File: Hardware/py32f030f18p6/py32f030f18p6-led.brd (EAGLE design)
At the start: 81.3 x 81.3 mm, 132 parts, among them IC2 AP2114HA-3.3TRG1, J10 455-1750-1-ND, J11 455-1750-1-ND, J12 455-1750-1-ND, J14 USB_MINI-B_SMT, J15 455-1750-1-ND, J16 455-1750-1-ND, J9 455-1750-1-ND, Q1 MMBT3904LT3G, Q10 MMBT3904LT3G, Q11 MMBT3904LT3G, Q12 MMBT3904LT3G, Q13 MMBT3904LT3G, Q14 MMBT3904LT3G, Q15 MMBT3904LT3G, Q16 MMBT3904LT3G, Q17 MMBT3904LT3G, Q18 MMBT3904LT3G, Q19 MMBT3904LT3G, Q2 MMBT3904LT3G, Q20 MMBT3904LT3G, Q21 MMBT3904LT3G, Q22 MMBT3904LT3G, Q23 MMBT3904LT3G, Q24 MMBT3904LT3G, Q25 MMBT3904LT3G, Q26 MMBT3904LT3G, Q27 MMBT3904LT3G, Q28 MMBT3904LT3G, Q29 MMBT3904LT3G, Q3 MMBT3904LT3G, Q30 MMBT3904LT3G, Q31 MMBT3904LT3G, Q32 MMBT3904LT3G, Q4 MMBT3904LT3G, Q5 MMBT3904LT3G, Q6 MMBT3904LT3G, Q7 MMBT3904LT3G, Q8 MMBT3904LT3G, Q9 MMBT3904LT3G, U1 TC74HC595AF(EL,F), U2 TC74HC595AF(EL,F), U3 TC74HC595AF(EL,F), U4 TC74HC595AF(EL,F), U5 TC74HC595AF(EL,F), U6 TC74HC595AF(EL,F), U7 TC74HC595AF(EL,F), U8 TC74HC595AF(EL,F)

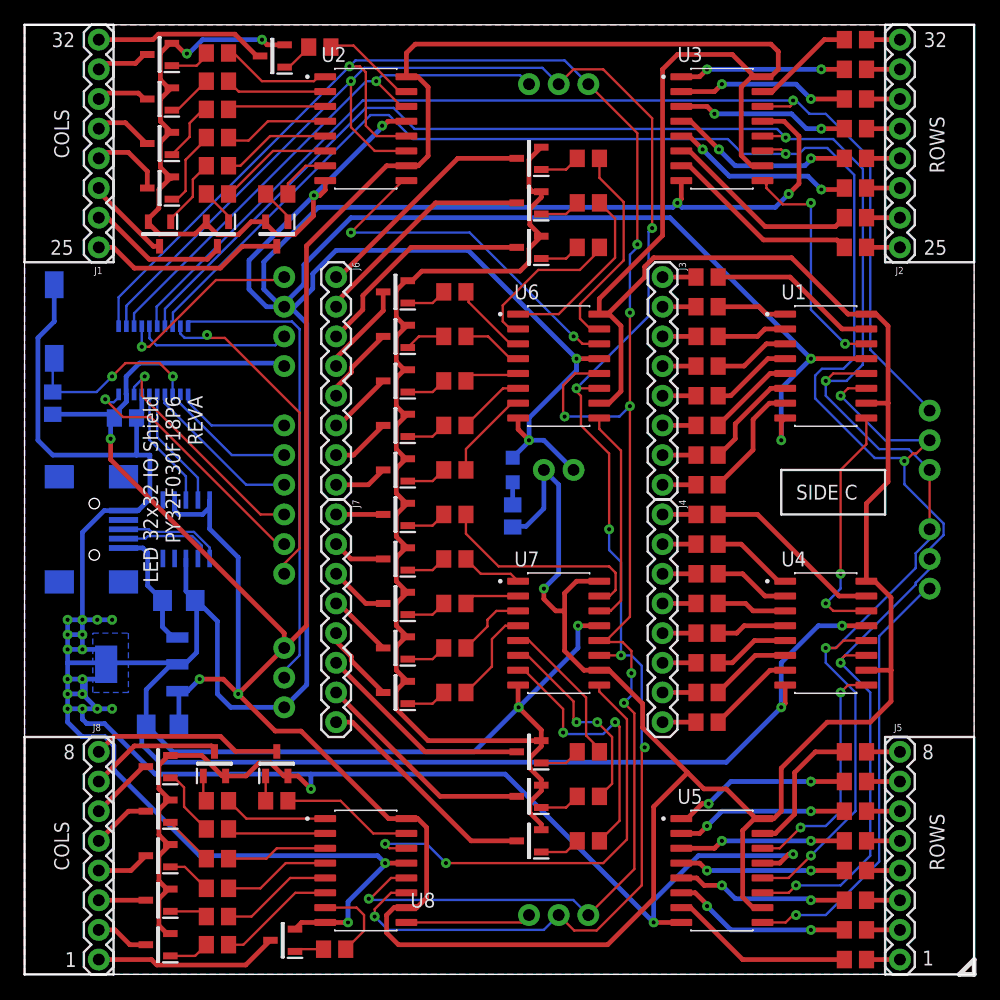
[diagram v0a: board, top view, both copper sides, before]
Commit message: Got row/col reversed
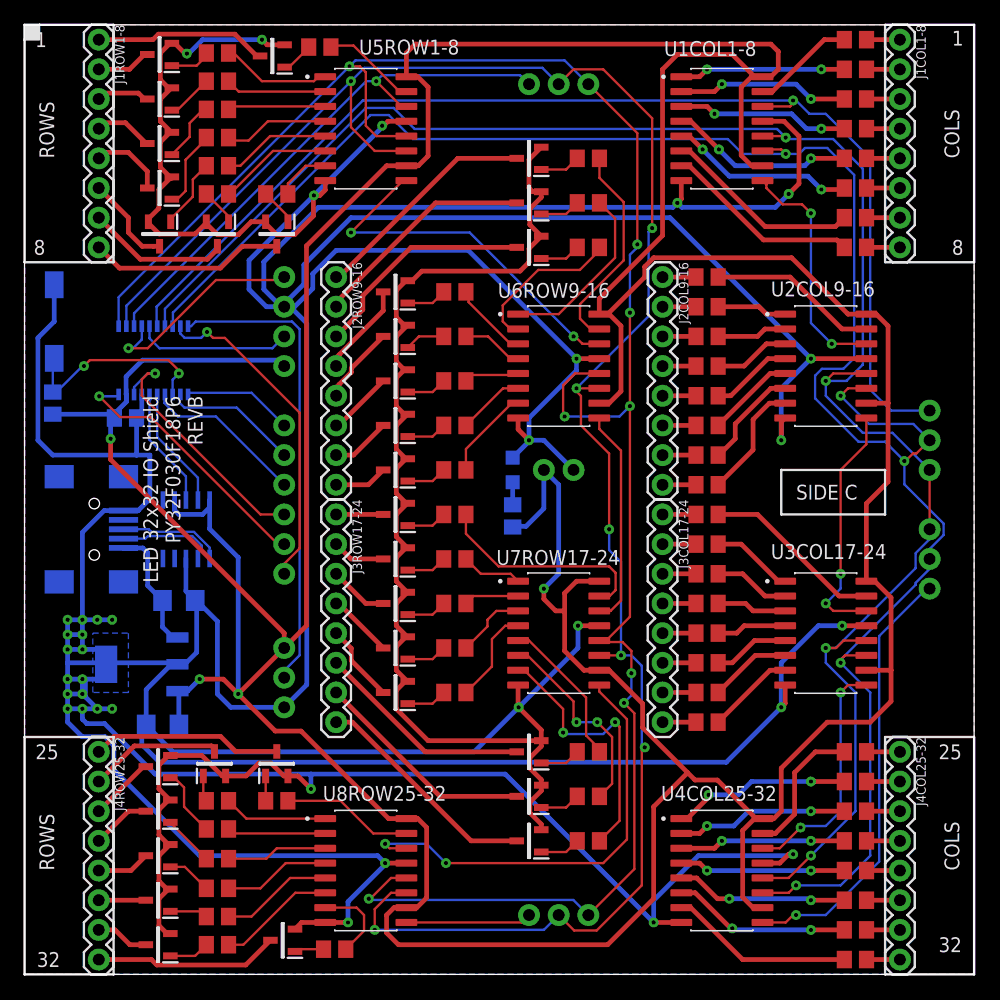
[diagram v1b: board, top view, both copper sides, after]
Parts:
- renumbered J1 to J1ROW1-8, J2 to J1COL1-8, J3 to J2COL9-16, J4 to J3COL17-24, J5 to J4COL25-32, J6 to J2ROW9-16, J7 to J3ROW17-24, J8 to J4ROW25-32, U1 to U2COL9-16, U2 to U5ROW1-8, U3 to U1COL1-8, U4 to U3COL17-24, U5 to U4COL25-32, U6 to U6ROW9-16, U7 to U7ROW17-24, U8 to U8ROW25-32
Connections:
- net COL_SCLK_IN renamed ROW_SCLK_IN
- net ROW_SLCK_IN renamed COL_SLCK_IN
- net COL_DATA_IN: now also J9.1, U$2.16, U1COL1-8.14; no longer J11.1, U$2.13, U5ROW1-8.14
- net COL_RCLK_IN: now also J10.3, J9.3, U$2.17, U1COL1-8.12, U2COL9-16.12, U3COL17-24.12, U4COL25-32.12; no longer J11.3, J12.3, U$2.11, U5ROW1-8.12, U6ROW9-16.12, U7ROW17-24.12, U8ROW25-32.12
- net ROW_DATA_IN: now also J11.1, U$2.13, U5ROW1-8.14; no longer J9.1, U$2.16, U1COL1-8.14
- net ROW_RCLK_IN: now also J11.3, J12.3, U$2.11, U5ROW1-8.12, U6ROW9-16.12, U7ROW17-24.12, U8ROW25-32.12; no longer J10.3, J9.3, U$2.17, U1COL1-8.12, U2COL9-16.12, U3COL17-24.12, U4COL25-32.12
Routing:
- net COL_DATA_IN: track 47.1 -> 100.7 mm
- net ROW_DATA_IN: track 98.8 -> 47.1 mm
- net ROW_RCLK_IN: track 158.1 -> 176.5 mm, vias 4 -> 8
- net COL_RCLK_IN: track 176.5 -> 158.1 mm, vias 8 -> 4
- net PA13-SWDIO: track 16.4 -> 18.5 mm
- net GPIO4: track 20.1 -> 22.1 mm
- net PF2-NRST: track 16.3 -> 17.5 mm
- net GPIO5: track 22.1 -> 22.9 mm
- net ROW_SCLK_IN: track 172.7 -> 173.4 mm
- net N$6: track 7.46 -> 8.02 mm
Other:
- board text added: "LED 32x32 IO Shield PY32F030F18P6 REVB"
- board text removed: "LED 32x32 IO Shield PY32F030F18P6 REVA"

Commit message: Added rx/tx breakout
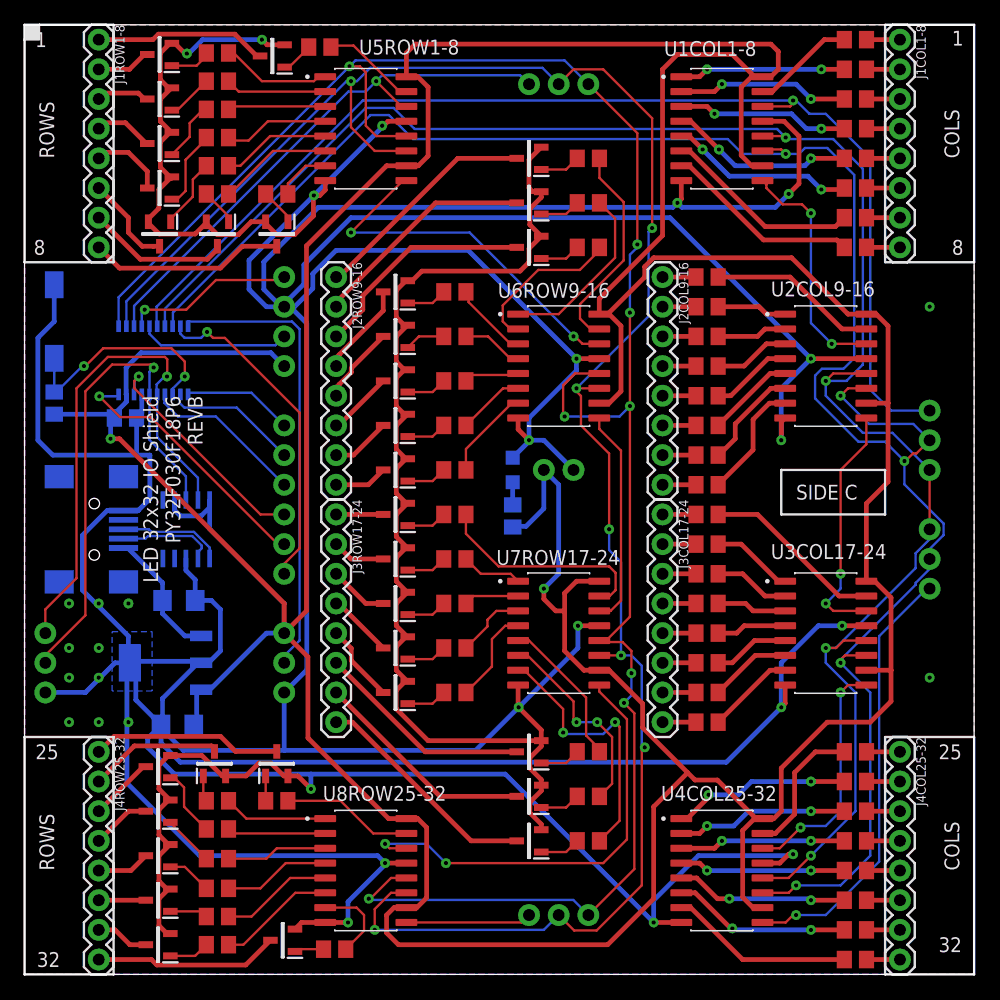
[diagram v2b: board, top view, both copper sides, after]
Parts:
- added J1: 455-1750-1-ND, SparkFun-Connectors:1X03
- moved IC2 2.04 mm to (12.1, 26.7)
- moved C9 1.27 mm to (13.1, 21.3)
- moved JP3 1.27 mm to (22.2, 29.2)
- moved R65 0.13 mm to (2.54, 48.9)
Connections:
- net GND: now also J1.1
- net PA2-U1TX: now also J1.3
- net PA3-U1RX: now also J1.2
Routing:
- net PA2-U1TX: track 10.5 -> 45.0 mm, vias 0 -> 1
- net GND: track 796.0 -> 761.4 mm, vias 35 -> 31
- net PA3-U1RX: track 10.3 -> 44.3 mm, vias 0 -> 1
- net +3V3: track 451.3 -> 446.5 mm, vias 4 -> 2
- net PA13-SWDIO: track 18.5 -> 14.6 mm
- net GPIO4: track 22.1 -> 20.2 mm
- net PF2-NRST: track 17.5 -> 19.3 mm
- net PF4-BOOT0: track 40.4 -> 39.3 mm
- net VBUS: track 10.8 -> 11.3 mm
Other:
- board text added: "PRG"
- board text added: "URX"
- board text added: "UTX"
- board text removed: "BOOT"
